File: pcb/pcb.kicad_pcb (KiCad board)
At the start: 6 copper layers, 172 parts, among them J1 mcu_debug, J1201 Conn_02x07_Top_Bottom, J1401 FPGA_JTAG, J301 Conn_02x07_Top_Bottom, J302 1658525-9, J601 DB15_Female_HighDensity, U201 TPS54325PWPR, U202 TPS54294PWP, U301 BGA112, U401 COM-09032, U666 XC7A75T-FTG256, U701 AS7C316098A-10TIN, Y1101 ECS-2520MV-080-BN-TR, Y301 Crystal_GND24

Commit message: connect onboard controller
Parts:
- moved C1102 240.2 mm to (-41.0, -77.0)
- moved C1103 240.2 mm to (-41.0, -72.8)
- moved C1101 240.2 mm to (-37.1, -66.4)
- moved C1104 240.2 mm to (-35.6, -74.7)
- moved C1106 240.2 mm to (-35.6, -77.7)
- moved C1107 240.2 mm to (-41.6, -69.2)
- moved C1113 240.2 mm to (-41.9, -62.6)
- moved C1114 240.2 mm to (-37.1, -69.4)
- moved C1115 240.2 mm to (-41.9, -60.1)
- moved R602 240.2 mm to (-41.7, -86.5)
- moved R613 240.2 mm to (-36.9, -86.5)
- moved Y1101 240.2 mm to (-41.4, -65.8)
- moved S401 179.4 mm to (223.4, 145.2)
- moved U666 172.0 mm to (270.4, -49.5)
- moved J601 160.7 mm to (84.8, -49.8)
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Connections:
- C1101 pad 2: +1V0 -> GND
- C1102 pad 2: +1V0 -> GND
- C1103 pad 2: +1V0 -> GND
- C1104 pad 2: +1V0 -> GND
- C1105 pad 2: +1V0 -> GND
- C1106 pad 2: +1V0 -> GND
- C1107 pad 2: +1V0 -> GND
- C1108 pad 2: +1V0 -> GND
- C1109 pad 2: +1V0 -> GND
- C1110 pad 2: +1V0 -> GND
- C1111 pad 2: +1V0 -> GND
- C1112 pad 2: +1V0 -> GND
- C1113 pad 2: +1V0 -> GND
- C1114 pad 2: +1V0 -> GND
- C1115 pad 2: +1V0 -> GND
- C1201 pad 2: +1V0 -> GND
- C1202 pad 2: +1V0 -> GND
- C1203 pad 2: +1V0 -> GND
- C1204 pad 2: +1V0 -> GND
- C1205 pad 2: +1V0 -> GND
- C1206 pad 2: +1V0 -> GND
- C1207 pad 2: +1V0 -> GND
- C1401 pad 1: +3V3 -> +3.3V
- C1401 pad 2: +1V0 -> GND
- C1402 pad 2: +1V0 -> GND
- C201 pad 2: +1V0 -> GND
- C202 pad 2: +1V0 -> GND
- C203 pad 2: +1V0 -> GND
- C204 pad 2: +1V0 -> GND
- C205 pad 2: +1V0 -> GND
- C206 pad 2: +1V0 -> GND
- C207 pad 2: +1V0 -> GND
- C208 pad 2: +1V0 -> GND
- C210 pad 2: +1V0 -> GND
- C211 pad 2: +1V0 -> GND
- C214 pad 2: +1V0 -> GND
- C215 pad 2: +1V0 -> GND
- C216 pad 2: +1V0 -> GND
- C217 pad 2: +1V0 -> GND
- C218 pad 2: +1V0 -> GND
- C219 pad 2: +1V0 -> GND
- C301 pad 2: +1V0 -> GND
- C302 pad 2: +1V0 -> GND
- C303 pad 2: +1V0 -> GND
- C304 pad 2: +1V0 -> GND
- C305 pad 2: +1V0 -> GND
- C306 pad 2: +1V0 -> GND
- C307 pad 2: +1V0 -> GND
- C308 pad 2: +1V0 -> GND
- C309 pad 2: +1V0 -> GND
- C310 pad 2: +1V0 -> GND
- C311 pad 2: +1V0 -> GND
- C501 pad 2: +1V0 -> GND
- C502 pad 2: +1V0 -> GND
- C503 pad 2: +1V0 -> GND
- C504 pad 2: +1V0 -> GND
- C505 pad 2: +1V0 -> GND
- C506 pad 2: +1V0 -> GND
- C507 pad 2: +1V0 -> GND
- C508 pad 2: +1V0 -> GND
- C509 pad 2: +1V0 -> GND
- C510 pad 2: +1V0 -> GND
- C511 pad 2: +1V0 -> GND
- C512 pad 2: +1V0 -> GND
- C513 pad 2: +1V0 -> GND
- C514 pad 2: +1V0 -> GND
- C515 pad 2: +1V0 -> GND
- C516 pad 2: +1V0 -> GND
- C517 pad 2: +1V0 -> GND
- C518 pad 2: +1V0 -> GND
- C519 pad 2: +1V0 -> GND
- C520 pad 2: +1V0 -> GND
- C521 pad 2: +1V0 -> GND
- C522 pad 2: +1V0 -> GND
- C523 pad 2: +1V0 -> GND
- C524 pad 2: +1V0 -> GND
- C701 pad 1: +1V0 -> GND
- C702 pad 1: +1V0 -> GND
- C801 pad 2: +1V0 -> GND
- C802 pad 2: +1V0 -> GND
- J1 pad 11: +1V0 -> GND
- J1 pad 13: +1V0 -> GND
- J1 pad 15: +1V0 -> GND
- J1 pad 17: +1V0 -> GND
- J1 pad 19: +1V0 -> GND
- J1201 pad 14: +1V0 -> GND
- J1401 pad 1: +1V0 -> GND
- J1401 pad 11: +1V0 -> GND
- J1401 pad 13: +1V0 -> GND
- J1401 pad 3: +1V0 -> GND
- J1401 pad 5: +1V0 -> GND
- J1401 pad 7: +1V0 -> GND
- J1401 pad 9: +1V0 -> GND
- J301 pad 14: +1V0 -> GND
- J302 pad 2: +1V0 -> GND
- J601 pad 10: +1V0 -> GND
- J601 pad 5: +1V0 -> GND
- J601 pad 6: +1V0 -> GND
- J601 pad 7: +1V0 -> GND
- J601 pad 8: +1V0 -> GND
- R1001 pad 2: +1V0 -> GND
- R1002 pad 2: +1V0 -> GND
- R1003 pad 2: +1V0 -> GND
- R1004 pad 2: +1V0 -> GND
- R202 pad 2: +1V0 -> GND
- R204 pad 2: +1V0 -> GND
- R208 pad 2: +1V0 -> GND
- R501 pad 2: +1V0 -> GND
- R502 pad 2: +1V0 -> GND
- R503 pad 2: +1V0 -> GND
- R504 pad 2: +1V0 -> GND
- S401 pad 1: +1V0 -> GND
- S402 pad 1: +1V0 -> GND
- S403 pad 1: +1V0 -> GND
- S404 pad 1: +1V0 -> GND
- S405 pad 1: +1V0 -> GND
- S406 pad 1: +1V0 -> GND
- U201 pad 15: +1V0 -> GND
- U201 pad 5: +1V0 -> GND
- U201 pad 8: +1V0 -> GND
- U201 pad 9: +1V0 -> GND
- U202 pad 13: +1V0 -> GND
- U202 pad 4: +1V0 -> GND
- U202 pad 8: +1V0 -> GND
- U202 pad EPAD: +1V0 -> GND
- U401 pad B2A: +1V0 -> GND
- U401 pad H3: +1V0 -> GND
- U401 pad V3: +1V0 -> GND
- U666 pad A1: +1V0 -> GND
- U666 pad A11: +1V0 -> GND
- U666 pad B8: +1V0 -> GND
- U666 pad C15: +1V0 -> GND
- U666 pad C5: +1V0 -> GND
- U666 pad D12: +1V0 -> GND
- U666 pad D2: +1V0 -> GND
- U666 pad E7: +3V3 -> +3.3V
- U666 pad E9: +1V0 -> GND
- U666 pad F10: +1V0 -> GND
- U666 pad F16: +1V0 -> GND
- U666 pad F6: +1V0 -> GND
- U666 pad G13: +1V0 -> GND
- U666 pad G3: +1V0 -> GND
- U666 pad G9: +1V0 -> GND
- U666 pad H6: +1V0 -> GND
- U666 pad H7: +1V0 -> GND
- U666 pad H8: +1V0 -> GND
- U666 pad J11: +1V0 -> GND
- U666 pad J7: +1V0 -> GND
- U666 pad J8: +1V0 -> GND
- U666 pad J9: +1V0 -> GND
- U666 pad K14: +1V0 -> GND
- U666 pad K4: +1V0 -> GND
- U666 pad K6: +1V0 -> GND
- U666 pad L1: +1V0 -> GND
- U666 pad L11: +1V0 -> GND
- U666 pad L6: +3V3 -> +3.3V
- U666 pad M10: +1V0 -> GND
- U666 pad M11: +1V0 -> GND
- U666 pad M3: +1V0 -> GND
- U666 pad M8: +1V0 -> GND
- U666 pad N15: +1V0 -> GND
- U666 pad N5: +1V0 -> GND
- U666 pad P12: +1V0 -> GND
- U666 pad P2: +1V0 -> GND
- U666 pad R4: +1V0 -> GND
- U666 pad R9: +1V0 -> GND
- U666 pad T1: +1V0 -> GND
- U666 pad T16: +1V0 -> GND
- U666 pad T6: +1V0 -> GND
- U701 pad 13: +1V0 -> GND
- U701 pad 37: +1V0 -> GND
- Y1101 pad 2: +1V0 -> GND
- Y301 pad 2: +1V0 -> GND
- Y301 pad 4: +1V0 -> GND
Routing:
- net bo_js_button_1: track 0.00 -> 146.8 mm, vias 0 -> 1
- net bo_js_vert_1: track 0.00 -> 118.2 mm, vias 0 -> 1
- net bo_js_hor_1: track 0.00 -> 112.0 mm, vias 0 -> 1
- net bo_button_1: track 0.00 -> 98.8 mm, vias 0 -> 2
- net con_hor_1: track 0.00 -> 92.3 mm, vias 0 -> 1
- net con_js_button: track 0.00 -> 91.0 mm, vias 0 -> 1
- net con_js_vert_1: track 0.00 -> 89.2 mm, vias 0 -> 1
- net js_gpio_5: track 0.00 -> 84.6 mm
- net bo_button_6: track 0.00 -> 84.3 mm, vias 0 -> 2
- net bo_button_5: track 0.00 -> 84.0 mm, vias 0 -> 2
- net bo_button_3: track 0.00 -> 69.1 mm, vias 0 -> 2
- net bo_button_2: track 0.00 -> 61.5 mm, vias 0 -> 2
- net bo_button_4: track 0.00 -> 46.9 mm, vias 0 -> 2
- net +1V0: track 8.15 -> 0.00 mm
- net +3.3V: track 0.00 -> 6.80 mm, vias 0 -> 6
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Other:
- board text added: "tror pinningen her er litt feil se breakout board"

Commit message: more traces
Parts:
- moved C302 121.1 mm to (180.1, 98.9)
- moved C301 120.4 mm to (175.0, 98.7)
- moved C510 28.2 mm to (198.5, 91.8)
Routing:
- net js_gpio_3: track 0.00 -> 91.6 mm, vias 0 -> 2
- net js_gpio_4: track 0.00 -> 89.2 mm, vias 0 -> 2
- net js_gpio_1: track 0.00 -> 88.5 mm, vias 0 -> 3
- net js_gpio_2: track 0.00 -> 84.7 mm, vias 0 -> 3
- net js_gpio_6: track 0.00 -> 84.6 mm, vias 0 -> 2
- net GND: track 0.00 -> 8.58 mm, vias 0 -> 9
- net +3.3V: track 6.80 -> 13.1 mm, vias 6 -> 11
- net Net-(C301-Pad1): track 0.00 -> 2.49 mm
- net bo_js_hor_1: track 112.0 -> 112.8 mm

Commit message: change footprint of connector
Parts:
- J301: value Conn_02x07_Top_Bottom -> Conn_02x05_Top_Bottom; footprint Connector_PinHeader_2.54mm:PinHeader_2x07_P2.54mm_Vertical -> Connector_PinHeader_2.54mm:PinHeader_2x05_P2.54mm_Vertical
- moved U201 208.7 mm to (60.0, -27.0)
- moved R204 191.9 mm to (195.0, -86.0)
- moved C501 178.9 mm to (35.6, 12.6)
- moved C502 178.9 mm to (52.3, 32.2)
- moved C503 178.9 mm to (52.3, 29.1)
- moved C504 178.9 mm to (47.0, 12.0)
- moved C505 178.9 mm to (61.9, 28.8)
- moved C506 178.9 mm to (52.3, 38.2)
- moved C508 178.9 mm to (35.0, 29.1)
- moved C509 178.9 mm to (57.1, 28.8)
- moved C512 178.9 mm to (35.0, 26.0)
- moved C514 178.9 mm to (35.0, 23.0)
- moved C517 178.9 mm to (69.1, 21.1)
- moved C518 178.9 mm to (64.3, 21.1)
- moved C520 178.9 mm to (53.5, 25.8)
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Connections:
- C502 pad 1: +1V0 -> +1V8
- C504 pad 1: +1V0 -> +1V8
- C506 pad 1: +1V0 -> +1V8
- C508 pad 1: +1V0 -> +1V8
- C510 pad 1: +1V0 -> +1V8
- C512 pad 1: +1V0 -> +1V8
- J301 pad 10: MCU_DEBUG_US0_MOSI -> GND
- J301 pad 5: /Mcu/MCU_GPIO_5 -> MCU_DEBUG_US0_MISO
- J301 pad 6: /Mcu/MCU_GPIO_6 -> MCU_DEBUG_US0_MOSI
- J301 pad 7: /Mcu/MCU_GPIO_7 -> MCU_DEBUG_US0_CLK
- J301 pad 8: /Mcu/MCU_GPIO_8 -> MCU_DEBUG_US0_CS
- J301 pad 9: MCU_DEBUG_US0_MISO -> +3.3V
- JP201 pad 1: +1V0 -> +1V8
- U666 pad F8: +1V0 -> GND
- U666 pad G10: +1V0 -> +1V8
- U666 pad G7: +1V0 -> GND
- U666 pad G8: +1V0 -> +1V8
- U666 pad J10: +1V0 -> +1V8
- U666 pad K11: +1V0 -> +1V8
- U666 pad L10: +1V0 -> +1V8
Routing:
- net MCU_DEBUG_US0_MISO: track 0.00 -> 106.5 mm, vias 0 -> 1
- net /Mcu/MCU_GPIO_4: track 0.00 -> 105.3 mm, vias 0 -> 1
- net /Mcu/MCU_GPIO_1: track 0.00 -> 103.7 mm, vias 0 -> 1
- net /Mcu/MCU_GPIO_3: track 0.00 -> 100.6 mm, vias 0 -> 1
- net /Mcu/MCU_GPIO_2: track 0.00 -> 95.1 mm, vias 0 -> 1
- net mcu_led4: track 0.00 -> 13.4 mm
- net mcu_led1: track 0.00 -> 10.4 mm
- net mcu_led3: track 0.00 -> 9.75 mm
- net mcu_led2: track 0.00 -> 8.93 mm
- net GND: track 8.58 -> 16.6 mm, vias 9 -> 13
- net Net-(D1001-Pad1): track 0.00 -> 3.17 mm
- net Net-(D1004-Pad1): track 0.00 -> 3.08 mm
- net Net-(D1003-Pad1): track 0.00 -> 3.08 mm
- net Net-(D1002-Pad1): track 0.00 -> 3.08 mm
- net +3.3V: track 13.1 -> 15.2 mm, vias 11 -> 12

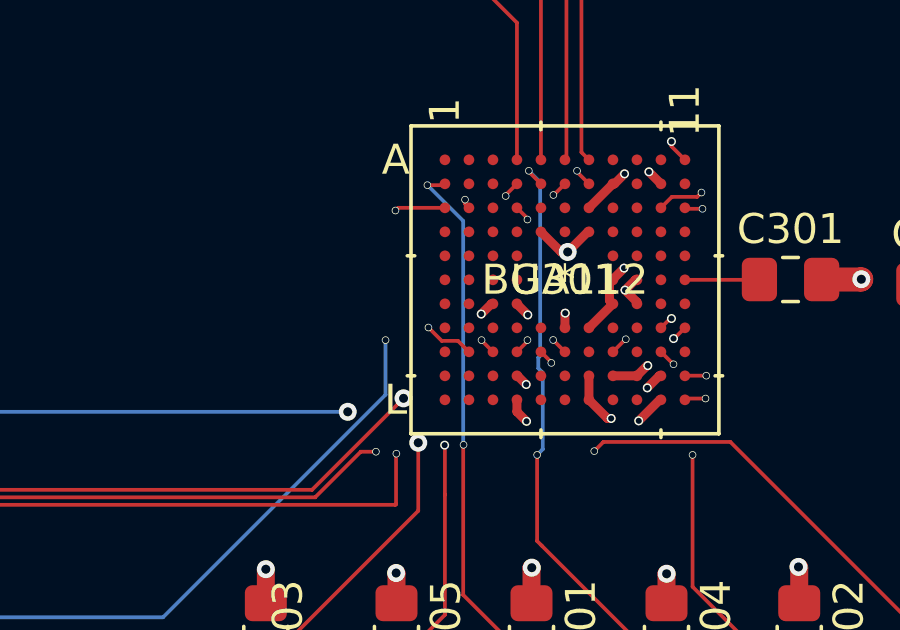
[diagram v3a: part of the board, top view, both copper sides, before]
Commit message: change footprint of debug_connector
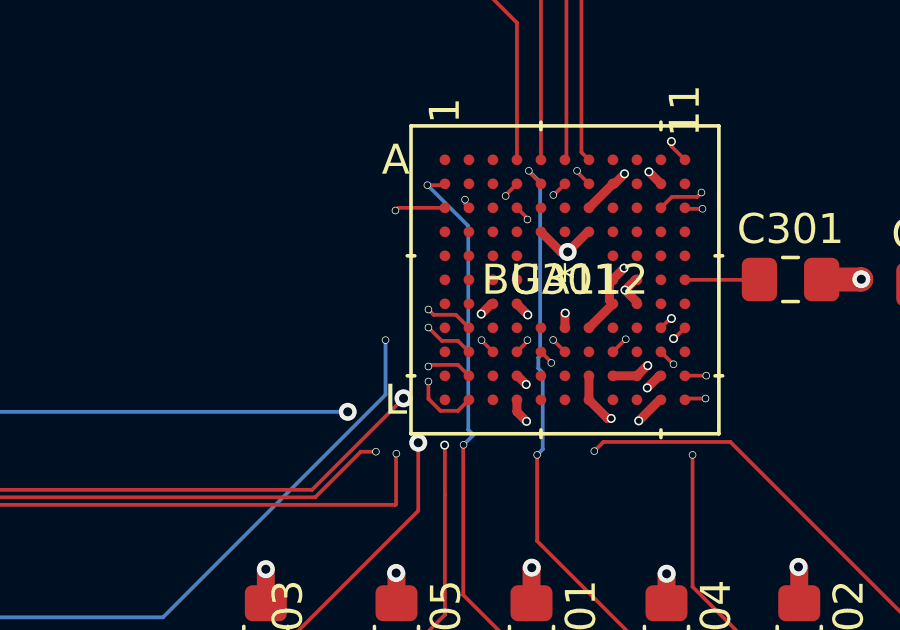
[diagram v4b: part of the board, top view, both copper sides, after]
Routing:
- net MCU_DEBUG_US0_CLK: track 0.00 -> 113.7 mm, vias 0 -> 1
- net MCU_DEBUG_US0_CS: track 55.0 -> 167.9 mm, vias 0 -> 1
- net MCU_DEBUG_US0_MOSI: track 0.00 -> 109.4 mm, vias 0 -> 1
- net MCU_DEBUG_US0_MISO: track 106.5 -> 111.2 mm
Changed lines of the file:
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@@
   (segment (start 163.3447 100.7447) (end 163.8847 100.7447) (width 0.125) (layer "F.Cu") (net 51))
   (via (at 162.9 100.3) (size 0.25) (drill 0.2) (layers "F.Cu" "B.Cu") (net 51))
-  (segment (start 161.1175 93.575393) (end 161.1175 98.5175) (width 0.125) (layer "In3.Cu") (net 51))
-  (segment (start 213.6575 52.1425) (end 173.2 92.6) (width 0.125) (layer "In3.Cu") (net 51))
-  (segment (start 161.1175 98.5175) (end 162.9 100.3) (width 0.125) (layer "In3.Cu") (net 51))
+  (segment (start 216.807108 48.992892) (end 216.8 48.985784) (width 0.125) (layer "In3.Cu") (net 51))
+  (segment (start 162.092893 92.6) (end 173.2 92.6) (width 0.125) (layer "In3.Cu") (net 51))
+  (segment (start 213.982666 27.882666) (end 213.982666 26.287666) (width 0.125) (layer "In3.Cu") (net 51))
+  (segment (start 216.8 48.985784) (end 216.8 29.6) (width 0.125) (layer "In3.Cu") (net 51))
+  (segment (start 173.2 92.6) (end 216.807108 48.992892) (width 0.125) (layer "In3.Cu") (net 51))
+  (segment (start 213.982666 26.287666) (end 212.62 24.925) (width 0.125) (layer "In3.Cu") (net 51))
+  (segment (start 215.7 29.6) (end 213.982666 27.882666) (width 0.125) (layer "In3.Cu") (net 51))
   (segment (start 212.62 24.925) (end 213.6575 25.9625) (width 0.125) (layer "In3.Cu") (net 51))
-  (segment (start 213.6575 25.9625) (end 213.6575 52.1425) (width 0.125) (layer "In3.Cu") (net 51))
-  (segment (start 162.092893 92.6) (end 161.1175 93.575393) (width 0.125) (layer "In3.Cu") (net 51))
-  (segment (start 173.2 92.6) (end 162.092893 92.6) (width 0.125) (layer "In3.Cu") (net 51))
+  (segment (start 162.9 100.3) (end 161.1175 98.5175) (width 0.125) (layer "In3.Cu") (net 51))
+  (segment (start 216.8 29.6) (end 215.7 29.6) (width 0.125) (layer "In3.Cu") (net 51))
+  (segment (start 161.1175 98.5175) (end 161.1175 93.575393) (width 0.125) (layer "In3.Cu") (net 51))
+  (segment (start 161.1175 93.575393) (end 162.092893 92.6) (width 0.125) (layer "In3.Cu") (net 51))
+  (segment (start 162.9 99.7) (end 163.0753 99.8753) (width 0.125) (layer "F.Cu") (net 52))
+  (segment (start 163.0753 99.8753) (end 163.8153 99.8753) (width 0.125) (layer "F.Cu") (net 52))
+  (segment (start 163.8153 99.8753) (end 164.25 100.31) (width 0.125) (layer "F.Cu") (net 52))
+  (via (at 162.9 99.7) (size 0.25) (drill 0.2) (layers "F.Cu" "B.Cu") (net 52))
+  (segment (start 160.8675 93.471839) (end 160.8675 98.6675) (width 0.125) (layer "In3.Cu") (net 52))
+  (segment (start 161.989339 92.35) (end 160.8675 93.471839) (width 0.125) (layer "In3.Cu") (net 52))
+  (segment (start 216.5 29.85) (end 216.5 48.946446) (width 0.125) (layer "In3.Cu") (net 52))
+  (segment (start 161.3 99.1) (end 161.3 99.311648) (width 0.125) (layer "In3.Cu") (net 52))
+  (segment (start 162.975 99.7) (end 162.9 99.7) (width 0.125) (layer "In3.Cu") (net 52))
+  (segment (start 216.173223 49.273223) (end 173.096446 92.35) (width 0.125) (layer "In3.Cu") (net 52))
+  (segment (start 215.7 29.85) (end 216.5 29.85) (width 0.125) (layer "In3.Cu") (net 52))
+  (segment (start 215.005 29.85) (end 215.7 29.85) (width 0.125) (layer "In3.Cu") (net 52))
+  (segment (start 172.9 92.35) (end 161.989339 92.35) (width 0.125) (layer "In3.Cu") (net 52))
+  (segment (start 216.5 48.946446) (end 216.173223 49.273223) (width 0.125) (layer "In3.Cu") (net 52))
+  (segment (start 161.3 99.311648) (end 162.720852 100.7325) (width 0.125) (layer "In3.Cu") (net 52))
+  (segment (start 163.3325 100.479148) (end 163.3325 100.0575) (width 0.125) (layer "In3.Cu") (net 52))
+  (segment (start 212.62 27.465) (end 215.005 29.85) (width 0.125) (layer "In3.Cu") (net 52))
+  (segment (start 163.3325 100.0575) (end 162.975 99.7) (width 0.125) (layer "In3.Cu") (net 52))
+  (segment (start 162.720852 100.7325) (end 163.079148 100.7325) (width 0.125) (layer "In3.Cu") (net 52))
+  (segment (start 160.8675 98.6675) (end 161.3 99.1) (width 0.125) (layer "In3.Cu") (net 52))
+  (segment (start 173.096446 92.35) (end 172.9 92.35) (width 0.125) (layer "In3.Cu") (net 52))
+  (segment (start 163.079148 100.7325) (end 163.3325 100.479148) (width 0.125) (layer "In3.Cu") (net 52))
+  (segment (start 163.8847 101.544699) (end 164.25 101.909999) (width 0.125) (layer "F.Cu") (net 53))
+  (segment (start 162.9 101.6) (end 162.955301 101.544699) (width 0.125) (layer "F.Cu") (net 53))
+  (segment (start 162.955301 101.544699) (end 163.8847 101.544699) (width 0.125) (layer "F.Cu") (net 53))
+  (via (at 162.9 101.6) (size 0.25) (drill 0.2) (layers "F.Cu" "B.Cu") (net 53))
+  (segment (start 161.885785 92.1) (end 160.6175 93.368286) (width 0.125) (layer "In3.Cu") (net 53))
+  (segment (start 216.25 30.75) (end 216.25 30.9) (width 0.125) (layer "In3.Cu") (net 53))
+  (segment (start 210.08 24.925) (end 211.1175 25.9625) (width 0.125) (layer "In3.Cu") (net 53))
+  (segment (start 211.1175 28.277834) (end 212.939666 30.1) (width 0.125) (layer "In3.Cu") (net 53))
+  (segment (start 171.5 92.1) (end 161.885785 92.1) (width 0.125) (layer "In3.Cu") (net 53))
+  (segment (start 172.992892 92.1) (end 171.5 92.1) (width 0.125) (layer "In3.Cu") (net 53))
+  (segment (start 216.25 48.842892) (end 216.196446 48.896446) (width 0.125) (layer "In3.Cu") (net 53))
+  (segment (start 160.6175 100.8175) (end 160.9 101.1) (width 0.125) (layer "In3.Cu") (net 53))
+  (segment (start 216.196446 48.896446) (end 172.992892 92.1) (width 0.125) (layer "In3.Cu") (net 53))
+  (segment (start 160.9 101.1) (end 161.4 101.6) (width 0.125) (layer "In3.Cu") (net 53))
+  (segment (start 215.6 30.1) (end 216.25 30.75) (width 0.125) (layer "In3.Cu") (net 53))
+  (segment (start 214.8 30.1) (end 215.6 30.1) (width 0.125) (layer "In3.Cu") (net 53))
+  (segment (start 211.1175 25.9625) (end 211.1175 28.277834) (width 0.125) (layer "In3.Cu") (net 53))
+  (segment (start 161.4 101.6) (end 162.9 101.6) (width 0.125) (layer "In3.Cu") (net 53))
+  (segment (start 212.939666 30.1) (end 214.8 30.1) (width 0.125) (layer "In3.Cu") (net 53))
+  (segment (start 160.6175 93.368286) (end 160.6175 100.8175) (width 0.125) (layer "In3.Cu") (net 53))
+  (segment (start 216.25 30.9) (end 216.25 48.842892) (width 0.125) (layer "In3.Cu") (net 53))
   (segment (start 176.822799 9.102799) (end 159.58 -8.14) (width 0.2) (layer "F.Cu") (net 54))
   (segment (start 194.2172 9.102799) (end 176.822799 9.102799) (width 0.125) (layer "F.Cu") (net 54))
+  (segment (start 163.8847 103.075299) (end 164.25 102.709999) (width 0.125) (layer "F.Cu") (net 54))
+  (segment (start 162.9 102.676612) (end 163.298687 103.075299) (width 0.125) (layer "F.Cu") (net 54))
+  (segment (start 163.298687 103.075299) (end 163.8847 103.075299) (width 0.125) (layer "F.Cu") (net 54))
+  (segment (start 162.9 102.1) (end 162.9 102.676612) (width 0.125) (layer "F.Cu") (net 54))
   (segment (start 217.34 3.619999) (end 216.9372 4.022799) (width 0.2) (layer "F.Cu") (net 54))
   (segment (start 194.2172 -3.597201) (end 194.2172 9.102799) (width 0.2) (layer "F.Cu") (net 54))
+  (via (at 162.9 102.1) (size 0.25) (drill 0.2) (layers "F.Cu" "B.Cu") (net 54))
+  (segment (start 161.782231 91.85) (end 160.3675 93.264733) (width 0.125) (layer "In3.Cu") (net 54))
+  (segment (start 161.546446 102.1) (end 162.9 102.1) (width 0.125) (layer "In3.Cu") (net 54))
+  (segment (start 171.5 91.85) (end 161.782231 91.85) (width 0.125) (layer "In3.Cu") (net 54))
+  (segment (start 216 30.9) (end 216 48.739338) (width 0.125) (layer "In3.Cu") (net 54))
+  (segment (start 215.4 30.35) (end 215.45 30.35) (width 0.125) (layer "In3.Cu") (net 54))
+  (segment (start 172.889338 91.85) (end 171.5 91.85) (width 0.125) (layer "In3.Cu") (net 54))
+  (segment (start 211.762919 30.35) (end 215.4 30.35) (width 0.125) (layer "In3.Cu") (net 54))
+  (segment (start 160.3675 93.264733) (end 160.3675 100.921054) (width 0.125) (layer "In3.Cu") (net 54))
+  (segment (start 215.319669 49.419669) (end 172.889338 91.85) (width 0.125) (layer "In3.Cu") (net 54))
+  (segment (start 210.08 28.667081) (end 211.762919 30.35) (width 0.125) (layer "In3.Cu") (net 54))
+  (segment (start 216 48.739338) (end 215.319669 49.419669) (width 0.125) (layer "In3.Cu") (net 54))
+  (segment (start 210.08 27.465) (end 210.08 28.667081) (width 0.125) (layer "In3.Cu") (net 54))
+  (segment (start 215.45 30.35) (end 216 30.9) (width 0.125) (layer "In3.Cu") (net 54))
+  (segment (start 160.3675 100.921054) (end 161.546446 102.1) (width 0.125) (layer "In3.Cu") (net 54))
   (segment (start 137.42 152.7947) (end 137.42 107.17) (width 0.125) (layer "F.Cu") (net 56))
   (segment (start 167.056451 100.714567) (end 167.056451 100.716451) (width 0.125) (layer "F.Cu") (net 56))
@@
   (via (at 164.07 104.21) (size 0.25) (drill 0.2) (layers "F.Cu" "B.Cu") (net 106))
   (via (at 162.8648 95.5548) (size 0.25) (drill 0.2) (layers "F.Cu" "B.Cu") (net 106))
-  (segment (start 164.0586 96.7486) (end 162.8648 95.5548) (width 0.125) (layer "B.Cu") (net 106))
-  (segment (start 164.0586 104.1986) (end 164.0586 96.7486) (width 0.125) (layer "B.Cu") (net 106))
-  (segment (start 164.07 104.21) (end 164.0586 104.1986) (width 0.125) (layer "B.Cu") (net 106))
+  (segment (start 164.2275 103.7075) (end 164.2275 96.9175) (width 0.125) (layer "B.Cu") (net 106))
+  (segment (start 164.2275 96.9175) (end 162.8648 95.5548) (width 0.125) (layer "B.Cu") (net 106))
+  (segment (start 164.07 104.21) (end 164.4 103.88) (width 0.125) (layer "B.Cu") (net 106))
+  (segment (start 164.4 103.88) (end 164.2275 103.7075) (width 0.125) (layer "B.Cu") (net 106))
   (segment (start 171.482199 96.3422) (end 171.449999 96.31) (width 0.125) (layer "F.Cu") (net 107))
   (segment (start 171.704 108.940282) (end 174.253718 111.49) (width 0.125) (layer "F.Cu") (net 107))
